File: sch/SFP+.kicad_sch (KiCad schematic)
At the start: 2 parts, among them J6 SFP+, J7 SFP+

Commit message: sfp+ sheet
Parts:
- added R1, R10, R2, R3, R4, R5, R6, R7, R8, R9: 4.7k, Resistor_SMD:R_0402_1005Metric, symbol Device:R
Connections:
- net Z2_FI3.10GbE_RX_N: now also J7.19 (TD-)
- net Z2_FI3.10GbE_RX_P: now also J7.18 (TD+)
- net Z2_FI3.10GbE_TX_N: now also J7.12 (RD-)
- net Z2_FI3.10GbE_TX_P: now also J7.13 (RD+)
- net Z2_FI3.TCDS2_RX_P: now also J6.18 (TD+)
- net Z2_FI3.TCDS2_TX_N: now also J6.12 (RD-)
- net Z2_FI3.TCDS2_TX_P: now also J6.13 (RD+)
- net GND: now reaches J6.1 (VeeT), J6.17 (VeeT), J6.20 (VeeT)
- net GND: now also J6.10 (VeeR), J6.11 (VeeR), J6.14 (VeeR), J7.1 (VeeT), J7.10 (VeeR), J7.11 (VeeR), J7.14 (VeeR), J7.17 (VeeT), J7.20 (VeeT)
- net +3V3: now reaches J6.15 (VccR)
- net +3V3: now also J6.16 (VccT), J7.15 (VccR), J7.16 (VccT), R1.1, R10.1, R2.1, R3.1, R4.1, R5.1, R6.1, R7.1, R8.1, R9.1
- net Z2_FI3.TCDS2_RX_N: now reaches J6.19 (TD-)
- net SC_SFP+_1.TX_FAULT: now reaches J6.2 (TX_FAULT)
- net SC_SFP+_1.TX_FAULT: now also R5.2
- net SC_SFP+_1.TX_DISABLE: now reaches J6.3 (TX_DISABLE)
- net SC_SFP+_1.SDA: now reaches J6.4 (SDA)
- net SC_SFP+_1.SDA: now also R3.2
- net SC_SFP+_1.SCL: now reaches J6.5 (SCL)
- net SC_SFP+_1.SCL: now also R2.2
- net SC_SFP+_1.MOD_ABS: now reaches J6.6 (MOD_ABS)
- net SC_SFP+_1.MOD_ABS: now also R1.2
- net SC_SFP+_1.RS0: now reaches J6.7 (RS0)
- net SC_SFP+_1.RX_LOS: now reaches J6.8 (RX_LOS)
- net SC_SFP+_1.RX_LOS: now also R4.2
- net SC_SFP+_1.RS1: now reaches J6.9 (RS1)
- net SC_SFP+_2.TX_FAULT: now reaches J7.2 (TX_FAULT)
- net SC_SFP+_2.TX_FAULT: now also R10.2
- net SC_SFP+_2.TX_DISABLE: now reaches J7.3 (TX_DISABLE)
- net SC_SFP+_2.SDA: now reaches J7.4 (SDA)
- net SC_SFP+_2.SDA: now also R8.2
- net SC_SFP+_2.SCL: now reaches J7.5 (SCL)
- net SC_SFP+_2.SCL: now also R7.2
- net SC_SFP+_2.MOD_ABS: now reaches J7.6 (MOD_ABS)
- net SC_SFP+_2.MOD_ABS: now also R6.2
- net SC_SFP+_2.RS0: now reaches J7.7 (RS0)
- net SC_SFP+_2.RX_LOS: now reaches J7.8 (RX_LOS)
- net SC_SFP+_2.RX_LOS: now also R9.2
- net SC_SFP+_2.RS1: now reaches J7.9 (RS1)
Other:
- note removed: "Cage x2 MOLEX 74754-0220 TE 2007262-1 or 2007263-1 Connector MOLEX 74441-0001 TE 1888247-1"
- company: (none) -> Karlsruhe Institute of Technology (KIT)
- title: (none) -> ATCA Simple Loopback HUB
- moved on the sheet: J6, J7

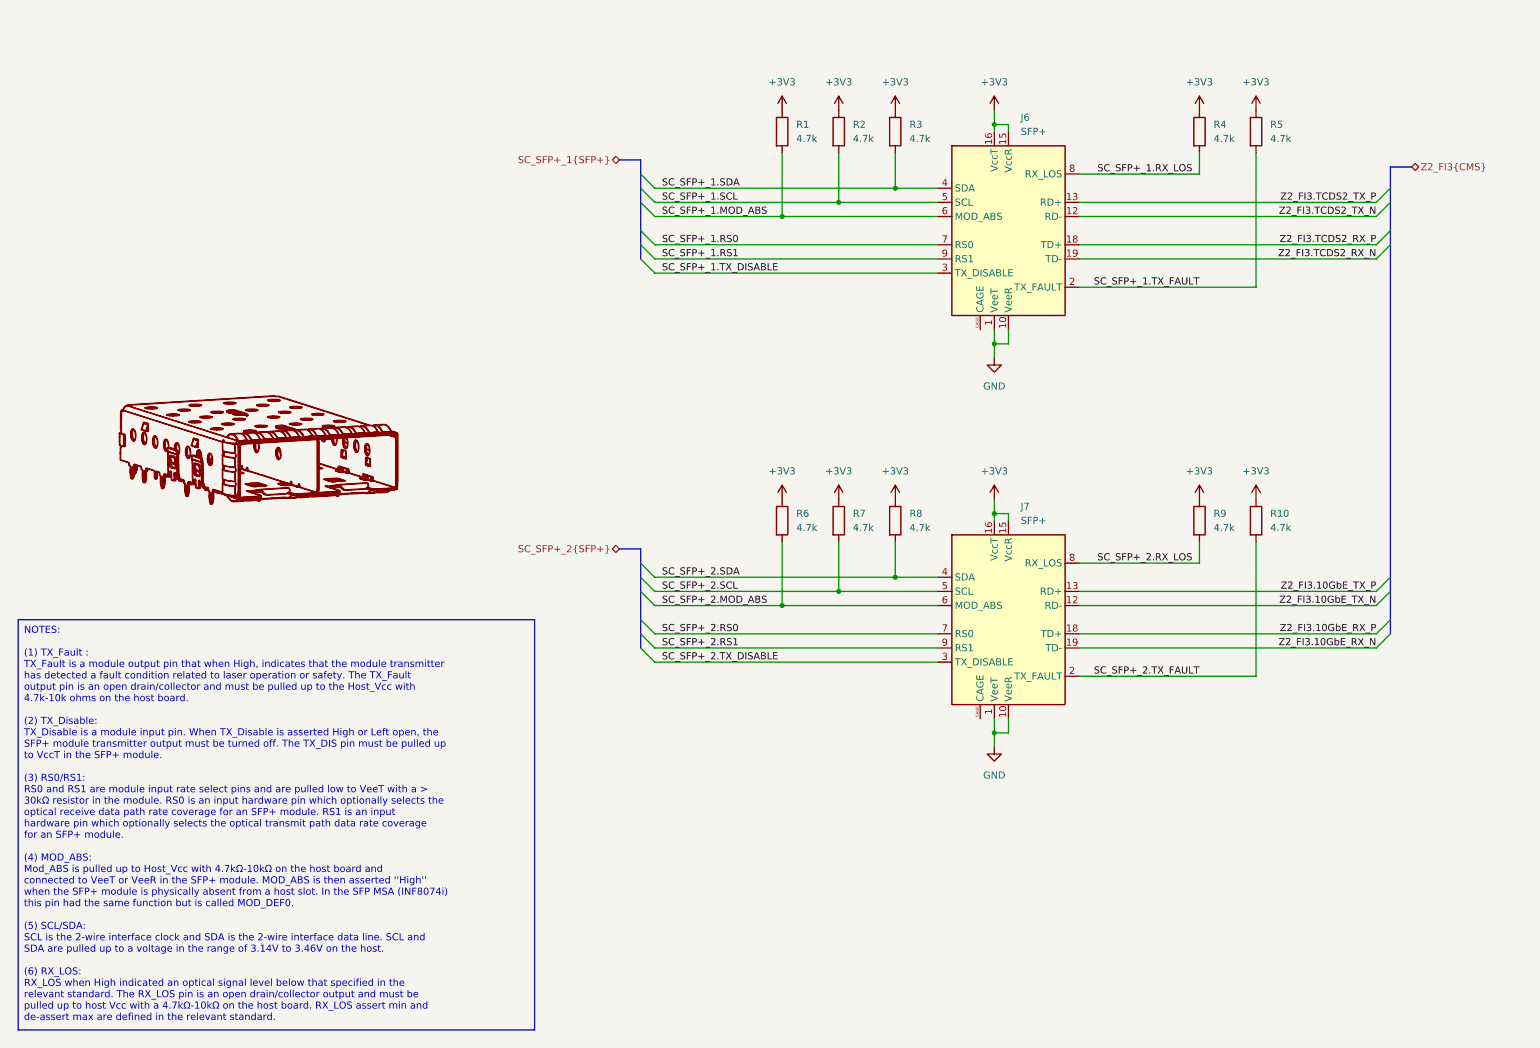
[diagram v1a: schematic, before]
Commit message: work on sc pll and pll sheet
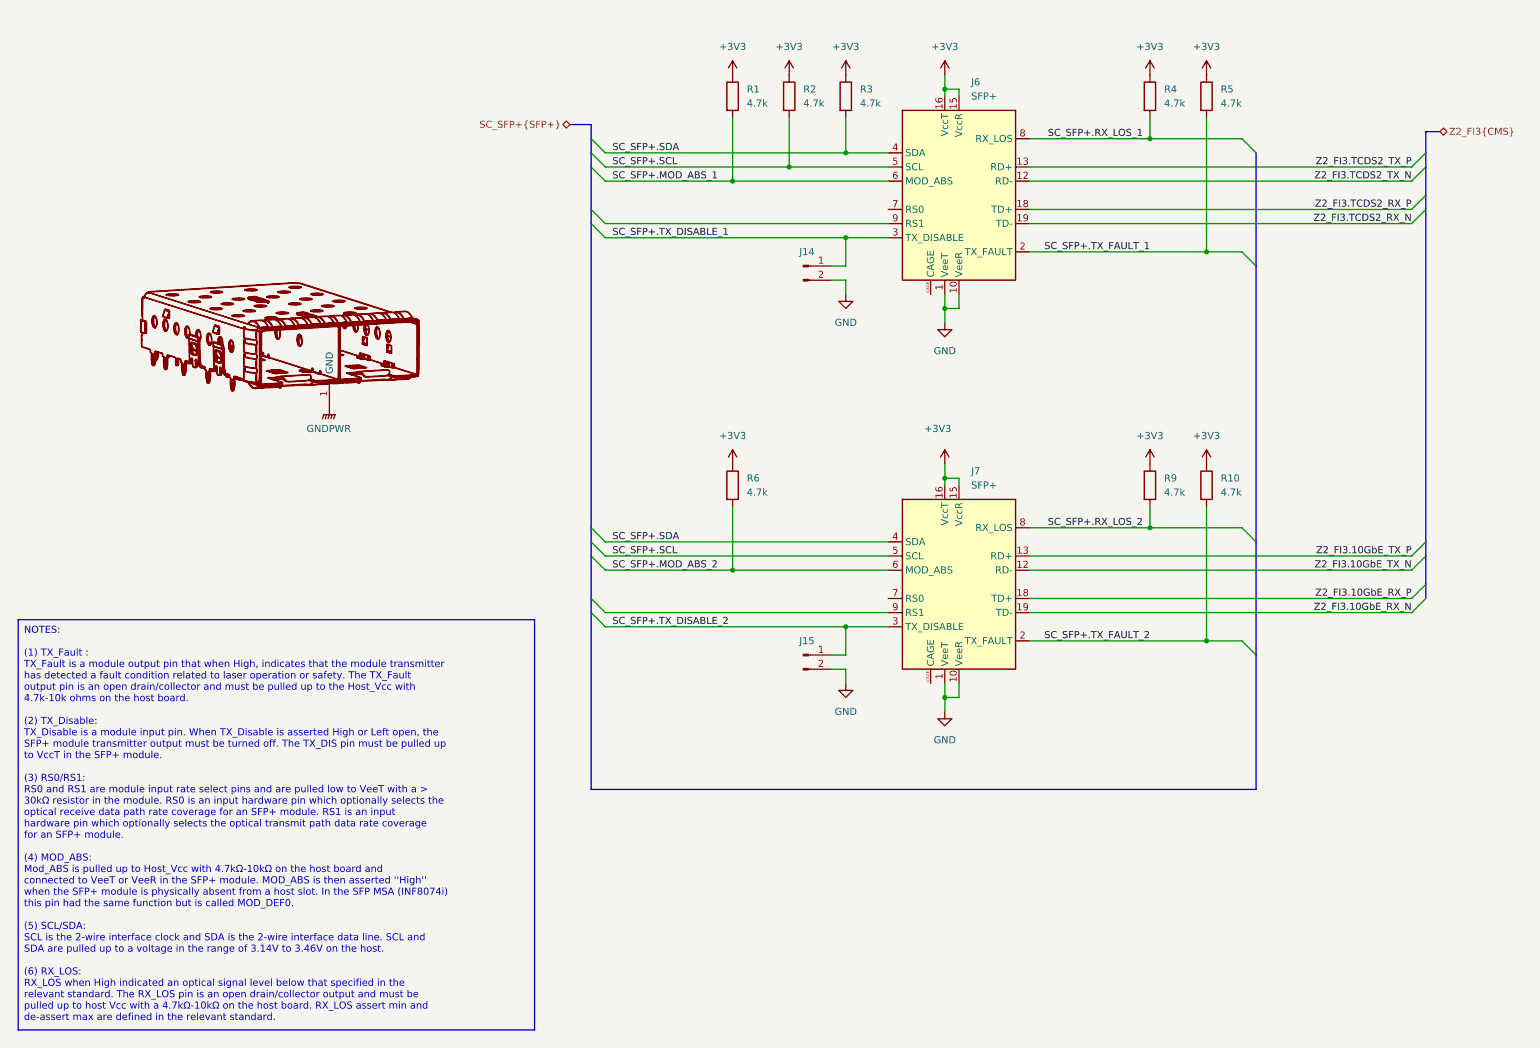
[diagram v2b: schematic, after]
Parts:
- removed R7, R8: 4.7k, Resistor_SMD:R_0402_1005Metric, symbol Device:R
- added J14, J15: Conn_01x02_Pin, Connector_PinHeader_2.54mm:PinHeader_1x02_P2.54mm_Vertical, symbol Connector:Conn_01x02_Pin
- added J16: TE 2007262-1, project:TE_2007263-1, symbol project:TE 2007262-1
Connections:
- net SC_SFP+_2.SCL is gone; now on net SC_SFP+.SCL: J7.5 (SCL)
- net SC_SFP+_2.SDA is gone; now on net SC_SFP+.SDA: J7.4 (SDA)
- net GND: now also J14.2 (Pin_2), J15.2 (Pin_2)
- net SC_SFP+_1.MOD_ABS renamed SC_SFP+.MOD_ABS_1
- net SC_SFP+_1.RS0: no longer names the net of J6.7 (RS0)
- net SC_SFP+_1.RS1: no longer names the net of J6.9 (RS1)
- net SC_SFP+_1.RX_LOS renamed SC_SFP+.RX_LOS_1
- net SC_SFP+_1.SCL renamed SC_SFP+.SCL
- net SC_SFP+_1.SDA renamed SC_SFP+.SDA
- net SC_SFP+_1.TX_DISABLE renamed SC_SFP+.TX_DISABLE_1
- net SC_SFP+.TX_DISABLE_1: now also J14.1 (Pin_1)
- net SC_SFP+_1.TX_FAULT renamed SC_SFP+.TX_FAULT_1
- net SC_SFP+_2.MOD_ABS renamed SC_SFP+.MOD_ABS_2
- net SC_SFP+_2.RS0: no longer names the net of J7.7 (RS0)
- net SC_SFP+_2.RS1: no longer names the net of J7.9 (RS1)
- net SC_SFP+_2.RX_LOS renamed SC_SFP+.RX_LOS_2
- net SC_SFP+_2.TX_DISABLE renamed SC_SFP+.TX_DISABLE_2
- net SC_SFP+.TX_DISABLE_2: now also J15.1 (Pin_1)
- net SC_SFP+_2.TX_FAULT renamed SC_SFP+.TX_FAULT_2
- new net GNDPWR: J16.1 (GND)
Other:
- moved on the sheet: J6, J7, R1, R10, R2, R3, R4, R5, R6, R9

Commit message: sch work
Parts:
- removed J14, J15: Conn_01x02_Pin, Connector_PinHeader_2.54mm:PinHeader_1x02_P2.54mm_Vertical, symbol Connector:Conn_01x02_Pin
- removed R2, R3: 4.7k, Resistor_SMD:R_0402_1005Metric, symbol Device:R
- added C17 (x2), C18 (x2): 0.1uF, Capacitor_SMD:C_0402_1005Metric, symbol Device:C
- added R20, R21: 4.7k, Resistor_SMD:R_0402_1005Metric, symbol Device:R
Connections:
- net +3V3: now also C17.2, C17.2, C18.2, C18.2
- net GND: now also C17.1, C17.1, C18.1, C18.1, R20.2, R21.2
- net SC_SFP+.MOD_ABS_1 renamed SC_SFP+_1.MOD_ABS_1
- net SC_SFP+.MOD_ABS_2 renamed SC_SFP+_2.MOD_ABS_2
- net SC_SFP+.RX_LOS_1 renamed SC_SFP+_1.RX_LOS_1
- net SC_SFP+.RX_LOS_2 renamed SC_SFP+_1.RX_LOS_2
- net SC_SFP+.SCL renamed SC_SFP+_1.SCL
- net SC_SFP+_1.SCL: no longer J7.5 (SCL)
- net SC_SFP+.SDA renamed SC_SFP+_1.SDA
- net SC_SFP+_1.SDA: no longer J7.4 (SDA)
- net SC_SFP+.TX_DISABLE_1 renamed SC_SFP+_1.TX_DISABLE_1
- net SC_SFP+_1.TX_DISABLE_1: now also R20.1
- net SC_SFP+.TX_DISABLE_2 renamed SC_SFP+_2.TX_DISABLE_2
- net SC_SFP+_2.TX_DISABLE_2: now also R21.1
- net SC_SFP+.TX_FAULT_1 renamed SC_SFP+_1.TX_FAULT_1
- net SC_SFP+.TX_FAULT_2 renamed SC_SFP+_2.TX_FAULT_2
- new net SC_SFP+_2.SCL: J7.5 (SCL)
- new net SC_SFP+_2.SDA: J7.4 (SDA)
- no-connect marks 0 -> 4
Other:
- moved on the sheet: J6, J7, R1, R10, R4, R5, R6, R9

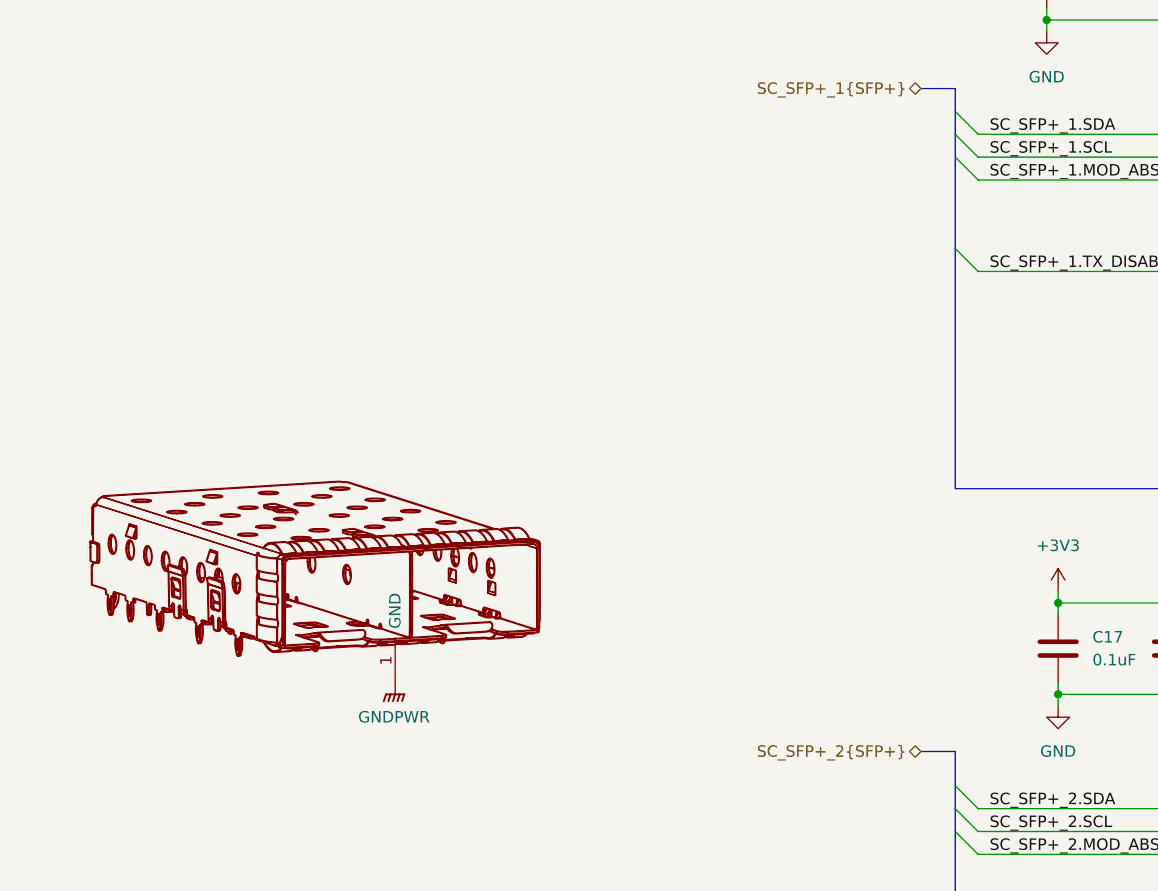
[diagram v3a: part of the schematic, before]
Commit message: started changes from review
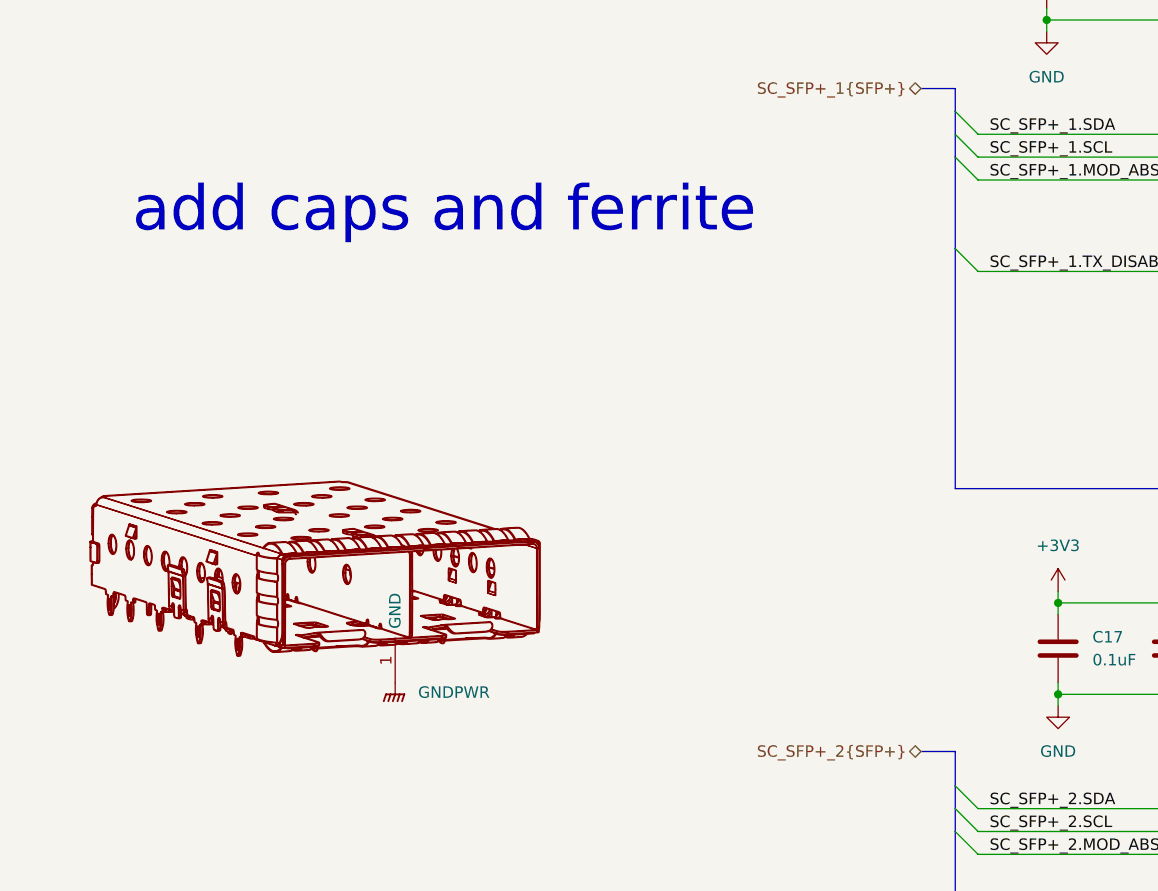
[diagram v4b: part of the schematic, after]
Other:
- note added: "add caps and ferrite"
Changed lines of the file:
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@@
     (effects (font (size 1.27 1.27)) (justify left top))
+  )
+  (text "add caps and ferrite" (at 25.4 57.15 0)
+    (effects (font (size 5 5)) (justify left bottom))
   )
   (label "SC_SFP+_2.MOD_ABS_2" (at 120.65 125.73 0) (fields_autoplaced)
@@
       (effects (font (size 1.27 1.27)) hide)
     )
-    (property "Value" "GNDPWR" (at 54.483 110.49 0)
-      (effects (font (size 1.27 1.27)))
+    (property "Value" "GNDPWR" (at 57.15 107.7468 0)
+      (effects (font (size 1.27 1.27)) (justify left))
     )
     (property "Footprint" "" (at 54.61 107.95 0)

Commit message: starting doing stackup calculations
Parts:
- added C15 (x4): 10uF, Capacitor_SMD:C_0603_1608Metric, symbol Device:C
- added FB3 (x4): FerriteBead, Inductor_SMD:L_0603_1608Metric, symbol Device:FerriteBead
- R20, R21: value 4.7k -> 0
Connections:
- net SC_SFP+_1.SCL is gone; now on net SC_SFP+_1.MOD_ABS_1: J6.5 (SCL)
- net SC_SFP+_1.SDA is gone; now on net SC_SFP+_1.MOD_ABS_1: J6.4 (SDA)
- net SC_SFP+_2.SCL is gone; now on net SC_SFP+_2.MOD_ABS_2: J7.5 (SCL)
- net SC_SFP+_2.SDA is gone; now on net SC_SFP+_2.MOD_ABS_2: J7.4 (SDA)
- net +3V3: now also C15.2, C15.2, C15.2, C15.2, FB3.1, FB3.1, FB3.1, FB3.1; no longer C17.2, C17.2, C18.2, C18.2, J6.15 (VccR), J6.16 (VccT), J7.15 (VccR), J7.16 (VccT)
- net GND: now also C15.1, C15.1, C15.1, C15.1
- net GNDPWR: now also J6.CAGE, J7.CAGE
- new net VccR1: C18.2, FB3.2, J6.15 (VccR)
- new net VccR2: C18.2, FB3.2, J7.15 (VccR)
- new net VccT1: C17.2, FB3.2, J6.16 (VccT)
- new net VccT2: C17.2, FB3.2, J7.16 (VccT)
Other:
- note removed: "add caps and ferrite"
- moved on the sheet: C17, C18, R1, R10, R4, R5, R6, R9

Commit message: update to v8
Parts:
- renumbered C15 to C102, C17 to C45, C18 to C46, C17 to C47, C18 to C48, C15 to C56, C15 to C64, C15 to C65, FB3 to FB10, FB3 to FB7, FB3 to FB8, FB3 to FB9

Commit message: routing PLLs
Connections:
- net SC_SFP+_1.MOD_ABS_1: no longer J6.4 (SDA), J6.5 (SCL)
- net SC_SFP+_2.MOD_ABS_2: no longer J7.4 (SDA), J7.5 (SCL)
- new net SC_SFP+_1.SCL: J6.5 (SCL)
- new net SC_SFP+_1.SDA: J6.4 (SDA)
- new net SC_SFP+_2.SCL: J7.5 (SCL)
- new net SC_SFP+_2.SDA: J7.4 (SDA)
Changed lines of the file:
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@@
+	)
+	(junction
+		(at 232.41 63.5)
+		(diameter 0)
+		(color 0 0 0 0)
+	)
+	(junction
+		(at 210.82 21.59)
+		(diameter 0)
+		(color 0 0 0 0)
+	)
+	(junction
+		(at 223.52 43.18)
+		(diameter 0)
+		(color 0 0 0 0)
+	)
+	(junction
+		(at 168.91 21.59)
+		(diameter 0)
+		(color 0 0 0 0)
+	)
+	(junction
+		(at 180.34 73.66)
+		(diameter 0)
+		(color 0 0 0 0)
 	)
 	(junction
@@
 	)
 	(junction
-		(at 232.41 63.5)
-		(diameter 0)
-		(color 0 0 0 0)
-	)
-	(junction
-		(at 210.82 21.59)
-		(diameter 0)
-		(color 0 0 0 0)
-	)
-	(junction
-		(at 223.52 43.18)
-		(diameter 0)
-		(color 0 0 0 0)
-	)
-	(junction
-		(at 168.91 21.59)
-		(diameter 0)
-		(color 0 0 0 0)
-	)
-	(junction
-		(at 180.34 73.66)
-		(diameter 0)
-		(color 0 0 0 0)
-	)
-	(junction
 		(at 210.82 96.52)
 		(diameter 0)
@@
 		)
 	)
+	(wire
+		(pts
+			(xy 119.38 125.73) (xy 120.65 125.73)
+		)
+		(stroke
+			(width 0)
+			(type default)
+		)
+	)
 	(bus
 		(pts
@@
 		(pts
 			(xy 119.38 50.8) (xy 120.65 50.8)
-		)
-		(stroke
-			(width 0)
-			(type default)
-		)
-	)
-	(wire
-		(pts
-			(xy 119.38 125.73) (xy 120.65 125.73)
 		)
 		(stroke
@@
 	)
 	(label "SC_SFP+_2.MOD_ABS_2"
-		(at 120.65 125.73 0)
+		(at 121.92 125.73 0)
 		(fields_autoplaced yes)
 		(effects
@@
 	)
 	(label "SC_SFP+_2.TX_DISABLE_2"
-		(at 120.65 135.89 0)
+		(at 121.92 135.89 0)
 		(fields_autoplaced yes)
 		(effects
@@
 	)
 	(label "SC_SFP+_1.SDA"
-		(at 120.65 45.72 0)
+		(at 121.92 45.72 0)
 		(fields_autoplaced yes)
 		(effects
@@
 	)
 	(label "SC_SFP+_1.TX_DISABLE_1"
-		(at 120.65 60.96 0)
+		(at 121.92 60.96 0)
 		(fields_autoplaced yes)
 		(effects
@@
 	)
 	(label "SC_SFP+_2.SDA"
-		(at 120.65 120.65 0)
+		(at 121.92 120.65 0)
 		(fields_autoplaced yes)
 		(effects
@@
 	)
 	(label "SC_SFP+_1.MOD_ABS_1"
-		(at 120.65 50.8 0)
+		(at 121.92 50.8 0)
 		(fields_autoplaced yes)
 		(effects
@@
 	)
 	(label "SC_SFP+_1.SCL"
-		(at 120.65 48.26 0)
+		(at 121.92 48.26 0)
 		(fields_autoplaced yes)
 		(effects
@@
 	)
 	(label "SC_SFP+_2.SCL"
-		(at 120.65 123.19 0)
-		(fields_autoplaced yes)
-		(effects
+		(at 121.92 123.19 0)
+		(fields_autoplaced yes)
+		(effects
